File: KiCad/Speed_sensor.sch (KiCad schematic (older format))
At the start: 69 parts, among them J1 USB_B_Micro, J2 SWD, U1 BQ24040DSQR, U2 TP1941U, U3 ST1PS02, U4 nRF52832-QFxx, U5 LIS2DH12, Y1 32,768kHz, Y2 32MHz

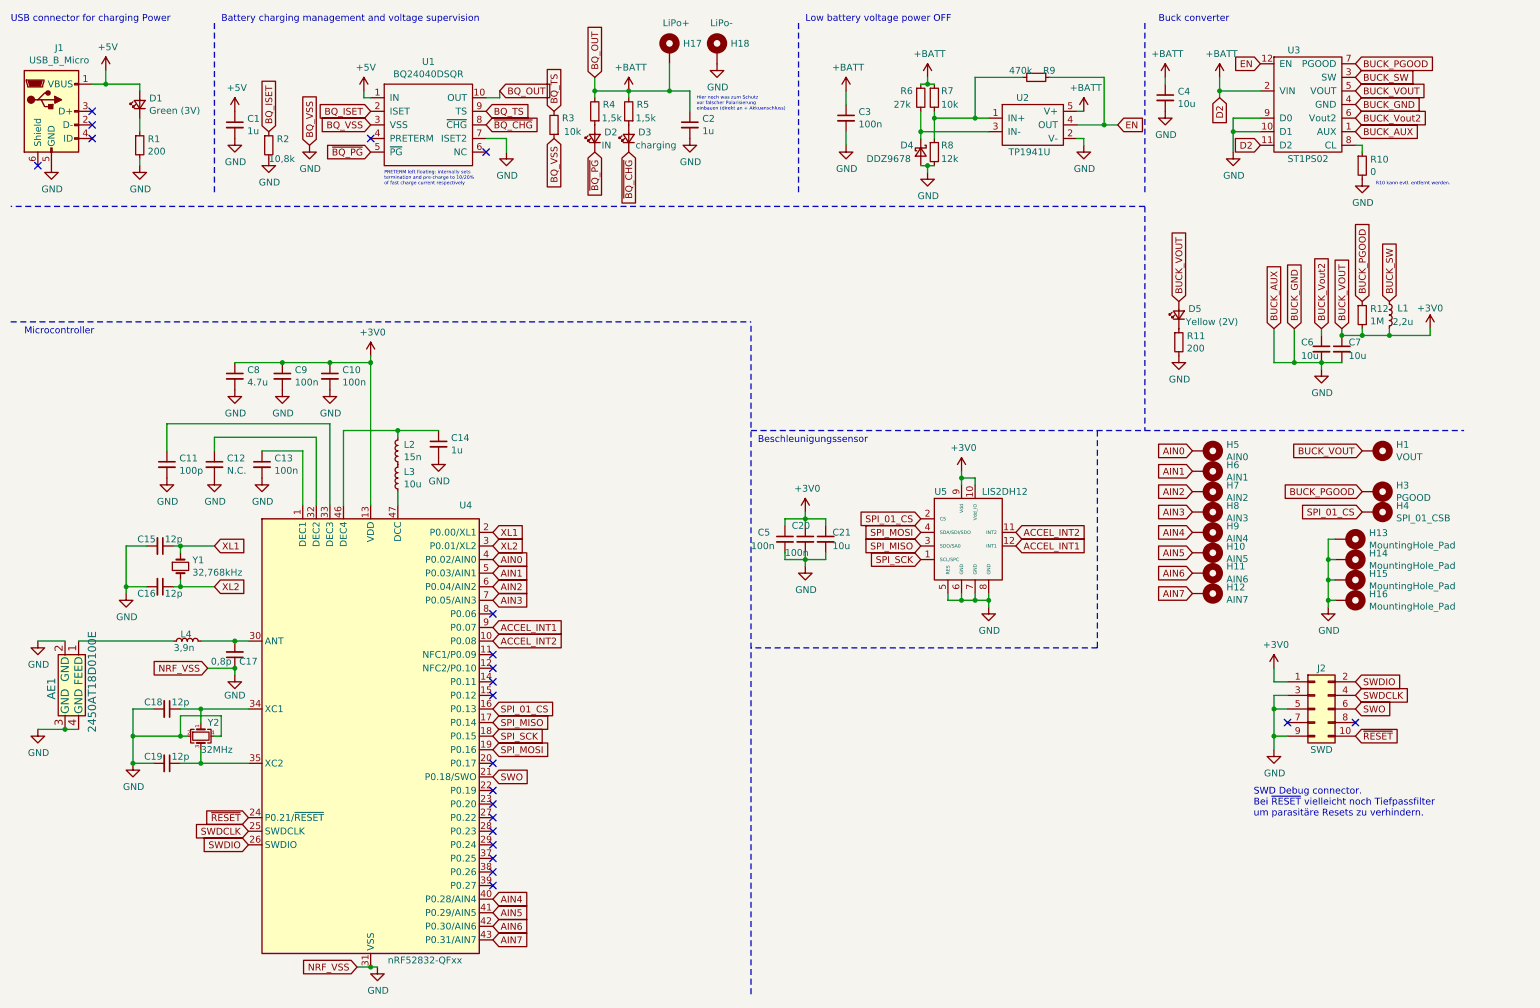
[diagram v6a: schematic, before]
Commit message: changed some labels in the .sch so all power stuff is labeled correctly
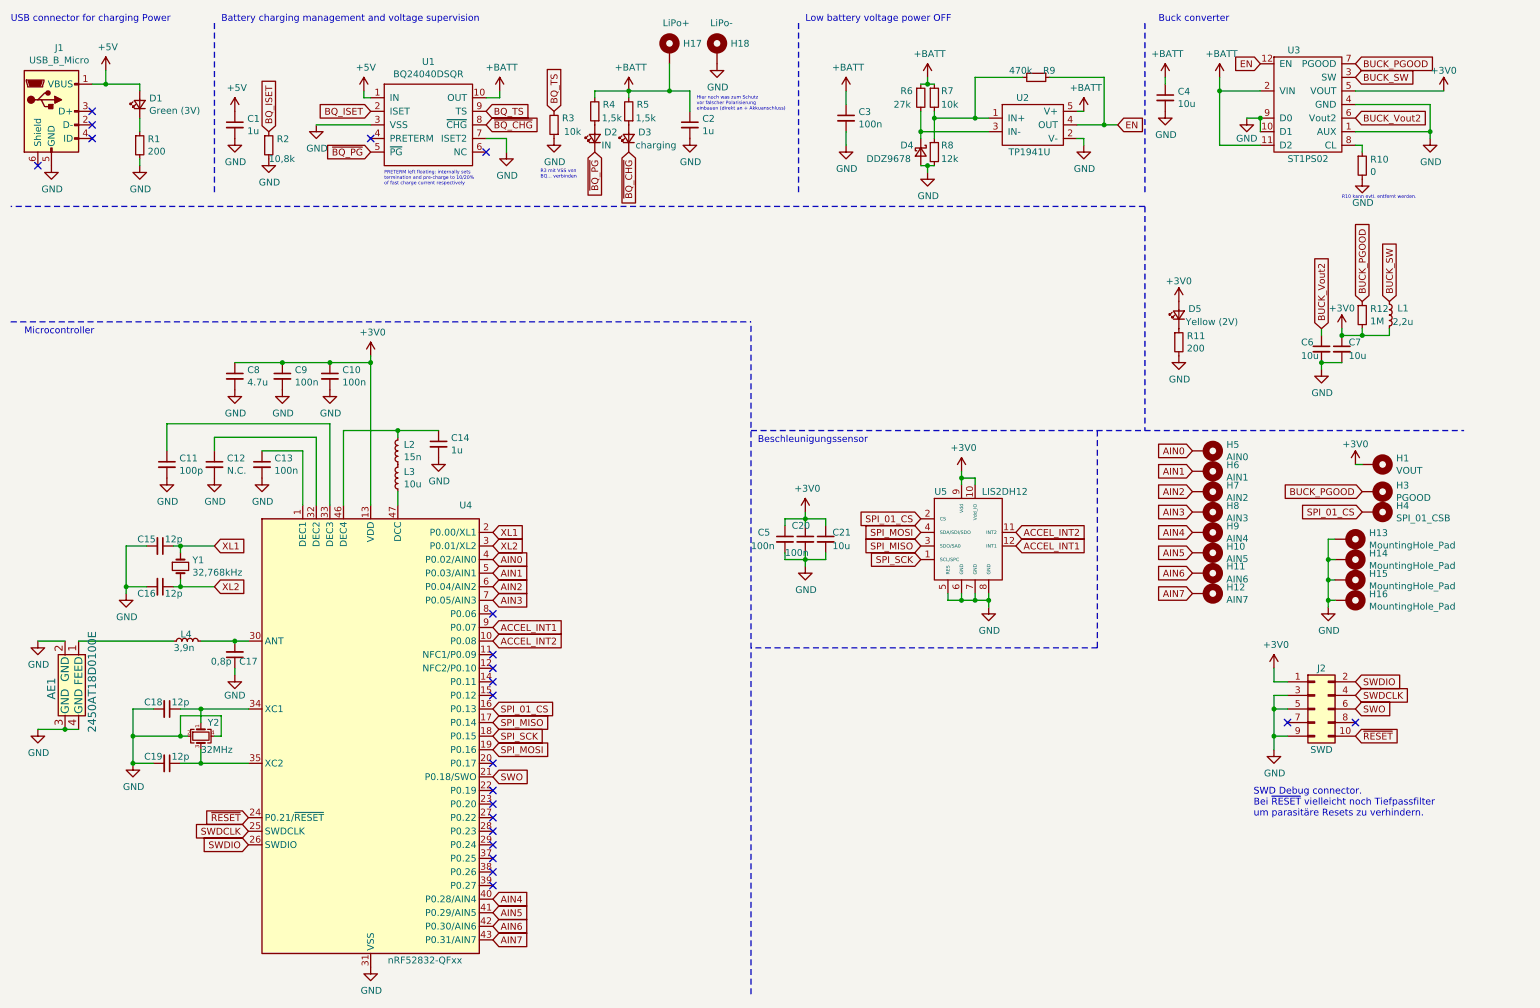
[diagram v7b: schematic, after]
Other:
- note added: "R3 mit VSS von \nBQ... verbinden"
- moved on the sheet: H1
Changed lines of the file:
@@
 L power:GND #PWR0101
 U 1 1 60833A00
-P 3200 7550
-F 0 "#PWR0101" H 3200 7300 50  0001 C CNN
-F 1 "GND" H 3205 7377 50  0000 C CNN
-F 2 "" H 3200 7550 50  0001 C CNN
-F 3 "" H 3200 7550 50  0001 C CNN
-	1    3200 7550
+P 3150 7550
+F 0 "#PWR0101" H 3150 7300 50  0001 C CNN
+F 1 "GND" H 3155 7377 50  0000 C CNN
+F 2 "" H 3150 7550 50  0001 C CNN
+F 3 "" H 3150 7550 50  0001 C CNN
+	1    3150 7550
 	1    0    0    -1
 $EndComp
@@
 Text Notes 600  2900 0    50   ~ 0
 Microcontroller
-Text GLabel 10450 3750 0    50   Input ~ 0
-BUCK_VOUT
 Text GLabel 4050 5650 2    50   Input ~ 0
 SPI_01_CS
@@
 L Mechanical:MountingHole_Pad H1
 U 1 1 609B0299
-P 10550 3750
-F 0 "H1" V 10504 3900 50  0000 L CNN
-F 1 "VOUT" V 10595 3900 50  0000 L CNN
-F 2 "TestPoint:TestPoint_Loop_D1.80mm_Drill1.0mm_Beaded" H 10550 3750 50  0001 C CNN
-F 3 "~" H 10550 3750 50  0001 C CNN
-	1    10550 3750
+P 10550 3850
+F 0 "H1" V 10504 4000 50  0000 L CNN
+F 1 "VOUT" V 10595 4000 50  0000 L CNN
+F 2 "TestPoint:TestPoint_Loop_D1.80mm_Drill1.0mm_Beaded" H 10550 3850 50  0001 C CNN
+F 3 "~" H 10550 3850 50  0001 C CNN
+	1    10550 3850
 	0    1    1    0
 $EndComp
@@
 Text GLabel 10400 5650 2    50   Input ~ 0
 SWO
-Text GLabel 9700 1500 0    50   Input ~ 0
-D2
 Text GLabel 9700 900  0    50   Input ~ 0
 EN
@@
 Text Notes 8950 600  0    50   ~ 0
 Buck converter
-Text GLabel 9400 1150 3    50   Input ~ 0
-D2
 $Comp
 L power:GND #PWR?
 U 1 1 609EC4A9
-P 9500 1550
+P 9600 1300
 AR Path="/608A57BF/609EC4A9" Ref="#PWR?"  Part="1"
 AR Path="/609EC4A9" Ref="#PWR029"  Part="1"
-F 0 "#PWR029" H 9500 1300 50  0001 C CNN
-F 1 "GND" H 9505 1377 50  0000 C CNN
-F 2 "" H 9500 1550 50  0001 C CNN
-F 3 "" H 9500 1550 50  0001 C CNN
-	1    9500 1550
-	1    0    0    -1
-$EndComp
-Wire Wire Line
-	9500 1400 9700 1400
-Wire Wire Line
-	9500 1300 9500 1400
-Connection ~ 9500 1400
-Wire Wire Line
-	9500 1400 9500 1550
-Text GLabel 10400 1100 2    50   Input ~ 0
-BUCK_VOUT
-Text GLabel 9100 2650 1    50   Input ~ 0
-BUCK_VOUT
-Wire Wire Line
-	9500 1300 9700 1300
+F 0 "#PWR029" H 9600 1050 50  0001 C CNN
+F 1 "GND" H 9600 1150 50  0000 C CNN
+F 2 "" H 9600 1300 50  0001 C CNN
+F 3 "" H 9600 1300 50  0001 C CNN
+	1    9600 1300
+	1    0    0    -1
+$EndComp
 Wire Wire Line
 	9400 1000 9400 1100
 Wire Wire Line
 	9400 1100 9700 1100
-Connection ~ 9400 1100
-Wire Wire Line
-	9400 1100 9400 1150
 $Comp
 L Device:C_Small C?
@@
 Text GLabel 10400 1000 2    50   Input ~ 0
 BUCK_SW
-Text GLabel 10400 1200 2    50   Input ~ 0
-BUCK_GND
 Text GLabel 10400 1300 2    50   Input ~ 0
 BUCK_Vout2
-Text GLabel 10400 1400 2    50   Input ~ 0
-BUCK_AUX
 $Comp
 L Device:R_Small R?
@@
 L power:GND #PWR09
 U 1 1 608BC5E0
-P 2700 1500
-F 0 "#PWR09" H 2700 1250 50  0001 C CNN
-F 1 "GND" H 2705 1327 50  0000 C CNN
-F 2 "" H 2700 1500 50  0001 C CNN
-F 3 "" H 2700 1500 50  0001 C CNN
-	1    2700 1500
-	1    0    0    -1
-$EndComp
-Text GLabel 4100 1100 2    50   Input ~ 0
-BQ_OUT
+P 2750 1350
+F 0 "#PWR09" H 2750 1100 50  0001 C CNN
+F 1 "GND" H 2755 1177 50  0000 C CNN
+F 2 "" H 2750 1350 50  0001 C CNN
+F 3 "" H 2750 1350 50  0001 C CNN
+	1    2750 1350
+	1    0    0    -1
+$EndComp
 Text GLabel 4000 1250 2    50   Input ~ 0
 BQ_TS
@@
 Wire Wire Line
 	4150 1450 4000 1450
-Text GLabel 3150 1350 0    50   Input ~ 0
-BQ_VSS
-Text GLabel 2700 1500 1    50   Input ~ 0
-BQ_VSS
-Text GLabel 4500 1450 3    50   Input ~ 0
-BQ_VSS
 Text GLabel 4500 1250 1    50   Input ~ 0
 BQ_TS
@@
 	-1   0    0    1
 $EndComp
-Text GLabel 4800 1000 1    50   Input ~ 0
-BQ_OUT
 Text GLabel 5050 1550 3    50   Input ~ 0
 ~BQ_CHG~
@@
 $EndComp
 Wire Wire Line
-	4800 1000 4800 1100
-Wire Wire Line
 	4800 1100 5050 1100
 Wire Wire Line
 	5050 1100 5050 1150
-Connection ~ 4800 1100
 Wire Wire Line
 	4800 1100 4800 1150
@@
 	1900 5150 2150 5150
 Connection ~ 2150 5150
-Text GLabel 3050 7550 0    50   Input ~ 0
-NRF_VSS
-Wire Wire Line
-	3050 7550 3150 7550
-Connection ~ 3150 7550
-Wire Wire Line
-	3150 7550 3200 7550
-Text GLabel 1950 5350 0    50   Input ~ 0
-NRF_VSS
 Wire Wire Line
 	2150 5350 2150 5400
-Wire Wire Line
-	2150 5350 1950 5350
-Connection ~ 2150 5350
 Wire Notes Line
 	2000 600  2000 1850
@@
 Text GLabel 10650 2650 1    50   Input ~ 0
 BUCK_SW
-Text GLabel 10300 2850 1    50   Input ~ 0
-BUCK_VOUT
-Text GLabel 9950 2850 1    50   Input ~ 0
-BUCK_GND
 Text GLabel 10150 2850 1    50   Input ~ 0
 BUCK_Vout2
@@
 L power:+3V0 #PWR033
 U 1 1 60CABFF4
-P 10950 2850
-F 0 "#PWR033" H 10950 2700 50  0001 C CNN
-F 1 "+3V0" H 10950 3000 50  0000 C CNN
-F 2 "" H 10950 2850 50  0001 C CNN
-F 3 "" H 10950 2850 50  0001 C CNN
-	1    10950 2850
-	1    0    0    -1
-$EndComp
-Wire Wire Line
-	10950 2850 10950 2900
+P 10300 2850
+F 0 "#PWR033" H 10300 2700 50  0001 C CNN
+F 1 "+3V0" H 10300 3000 50  0000 C CNN
+F 2 "" H 10300 2850 50  0001 C CNN
+F 3 "" H 10300 2850 50  0001 C CNN
+	1    10300 2850
+	1    0    0    -1
+$EndComp
 Connection ~ 10300 2900
-Wire Wire Line
-	9950 2850 9950 3100
 $Comp
 L Device:L_Small L1
@@
 	10300 2900 10450 2900
 Connection ~ 10450 2900
-Connection ~ 10650 2900
 Wire Wire Line
 	10450 2900 10650 2900
-Wire Wire Line
-	10650 2900 10950 2900
-Connection ~ 9950 3100
-Wire Wire Line
-	9950 3100 10150 3100
-Text GLabel 9800 2850 1    50   Input ~ 0
-BUCK_AUX
-Wire Wire Line
-	9800 2850 9800 3100
-Wire Wire Line
-	9800 3100 9950 3100
 Text GLabel 4050 7050 2    50   Input ~ 0
 AIN4
@@
 Wire Wire Line
 	1750 5700 2050 5700
-Text Notes 10550 1800 0    25   ~ 0
+Text Notes 10300 1900 0    25   ~ 0
 R10 kann evtl. entfernt werden.
 $Comp
@@
 Wire Wire Line
 	4100 1150 4000 1150
+$Comp
+L power:+BATT #PWR037
+U 1 1 60A5CE9C
+P 4100 1100
+AR Path="/60A5CE9C" Ref="#PWR037"  Part="1"
+AR Path="/608A57BF/60A5CE9C" Ref="#PWR?"  Part="1"
+F 0 "#PWR037" H 4100 950 50  0001 C CNN
+F 1 "+BATT" H 4115 1273 50  0000 C CNN
+F 2 "" H 4100 1100 50  0001 C CNN
+F 3 "" H 4100 1100 50  0001 C CNN
+	1    4100 1100
+	1    0    0    -1
+$EndComp
+$Comp
+L power:+3V0 #PWR040
+U 1 1 60A5D75E
+P 11050 1100
+F 0 "#PWR040" H 11050 950 50  0001 C CNN
+F 1 "+3V0" H 11050 1250 50  0000 C CNN
+F 2 "" H 11050 1100 50  0001 C CNN
+F 3 "" H 11050 1100 50  0001 C CNN
+	1    11050 1100
+	1    0    0    -1
+$EndComp
+Wire Wire Line
+	10400 1100 11050 1100
+$Comp
+L power:+3V0 #PWR038
+U 1 1 60A6E034
+P 9100 2650
+F 0 "#PWR038" H 9100 2500 50  0001 C CNN
+F 1 "+3V0" H 9100 2800 50  0000 C CNN
+F 2 "" H 9100 2650 50  0001 C CNN
+F 3 "" H 9100 2650 50  0001 C CNN
+	1    9100 2650
+	1    0    0    -1
+$EndComp
+$Comp
+L power:+3V0 #PWR039
+U 1 1 60A6F470
+P 10400 3850
+F 0 "#PWR039" H 10400 3700 50  0001 C CNN
+F 1 "+3V0" H 10400 4000 50  0000 C CNN
+F 2 "" H 10400 3850 50  0001 C CNN
+F 3 "" H 10400 3850 50  0001 C CNN
+	1    10400 3850
+	1    0    0    -1
+$EndComp
+Wire Wire Line
+	10400 3850 10450 3850
+Wire Wire Line
+	2750 1350 3150 1350
+$Comp
+L power:GND #PWR041
+U 1 1 60A8BA9E
+P 4500 1450
+F 0 "#PWR041" H 4500 1200 50  0001 C CNN
+F 1 "GND" H 4505 1277 50  0000 C CNN
+F 2 "" H 4500 1450 50  0001 C CNN
+F 3 "" H 4500 1450 50  0001 C CNN
+	1    4500 1450
+	1    0    0    -1
+$EndComp
+Text Notes 4400 1750 0    25   ~ 0
+R3 mit VSS von \nBQ... verbinden
+$Comp
+L power:GND #PWR?
+U 1 1 60A8E087
+P 10950 1450
+AR Path="/608A57BF/60A8E087" Ref="#PWR?"  Part="1"
+AR Path="/60A8E087" Ref="#PWR042"  Part="1"
+F 0 "#PWR042" H 10950 1200 50  0001 C CNN
+F 1 "GND" H 10955 1277 50  0000 C CNN
+F 2 "" H 10950 1450 50  0001 C CNN
+F 3 "" H 10950 1450 50  0001 C CNN
+	1    10950 1450
+	1    0    0    -1
+$EndComp
+Wire Wire Line
+	10400 1200 10950 1200
+Wire Wire Line
+	10950 1200 10950 1400
+Wire Wire Line
+	10400 1400 10950 1400
+Connection ~ 10950 1400
+Wire Wire Line
+	10950 1400 10950 1450
+Wire Wire Line
+	9700 1400 9700 1300
+Wire Wire Line
+	9600 1300 9700 1300
+Connection ~ 9700 1300
+Wire Wire Line
+	9700 1500 9400 1500
+Wire Wire Line
+	9400 1500 9400 1100
+Connection ~ 9400 1100
 $EndSCHEMATC

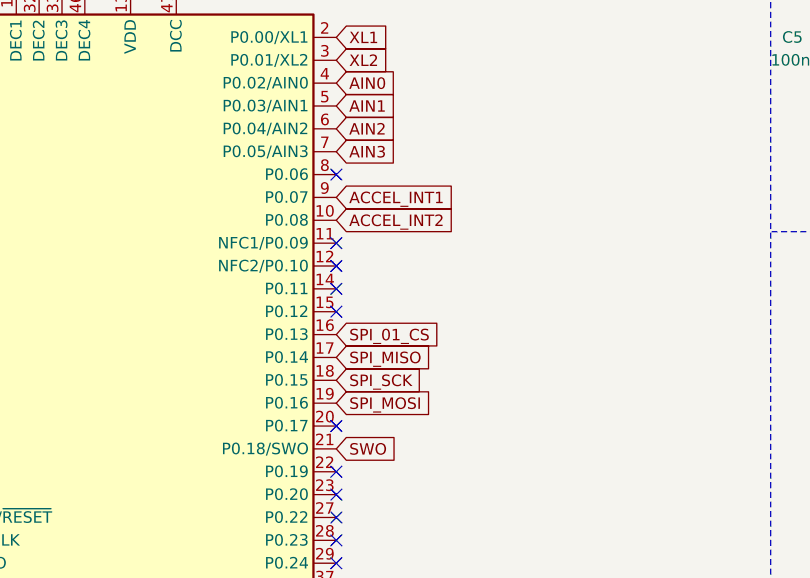
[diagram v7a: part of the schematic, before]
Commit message: changed which GPIO pins are used for SPI
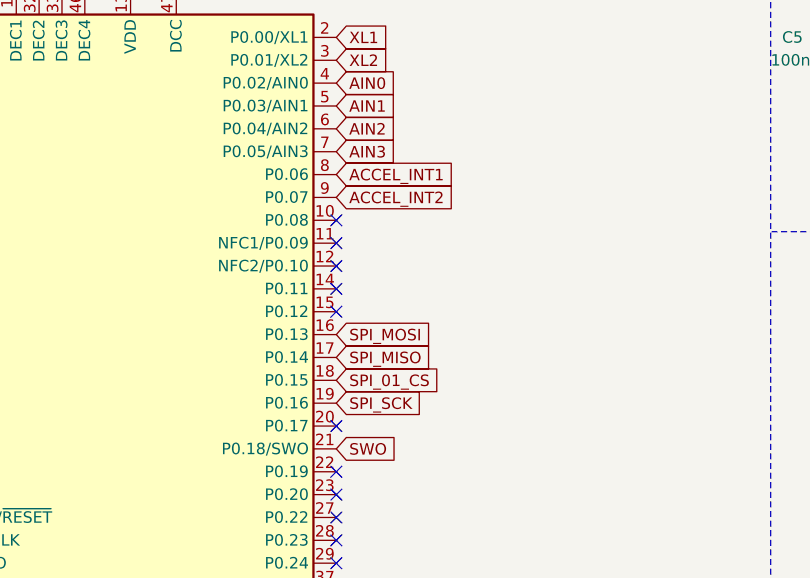
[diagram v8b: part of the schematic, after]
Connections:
- net ACCEL_INT1: now also U4.8 (P0.06); no longer U4.9 (P0.07)
- net ACCEL_INT2: now also U4.9 (P0.07); no longer U4.10 (P0.08)
- net SPI_01_CS: now also U4.18 (P0.15); no longer U4.16 (P0.13)
- net SPI_MOSI: now also U4.16 (P0.13); no longer U4.19 (P0.16)
- net SPI_SCK: now also U4.19 (P0.16); no longer U4.18 (P0.15)
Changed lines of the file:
@@
 Text Notes 600  2900 0    50   ~ 0
 Microcontroller
-Text GLabel 4050 5650 2    50   Input ~ 0
+Text GLabel 4050 5850 2    50   Input ~ 0
 SPI_01_CS
 Text GLabel 4050 5750 2    50   Input ~ 0
 SPI_MISO
-Text GLabel 4050 5950 2    50   Input ~ 0
+Text GLabel 4050 5650 2    50   Input ~ 0
 SPI_MOSI
 Text Notes 6000 3700 0    50   ~ 0
@@
 	0    1    1    0
 $EndComp
-Text GLabel 4050 5850 2    50   Input ~ 0
+Text GLabel 4050 5950 2    50   Input ~ 0
 SPI_SCK
 Text GLabel 4050 6150 2    50   Input ~ 0
@@
 Text GLabel 4050 4750 2    50   Input ~ 0
 AIN2
-Text GLabel 4050 4850 2    50   Input ~ 0
-AIN3
 Text GLabel 2000 4450 2    50   Input ~ 0
 XL1
@@
 Text GLabel 7200 4250 0    50   Input ~ 0
 SPI_01_CS
+Text GLabel 4050 4950 2    50   Input ~ 0
+ACCEL_INT1
 Text GLabel 4050 5050 2    50   Input ~ 0
-ACCEL_INT1
-Text GLabel 4050 5150 2    50   Input ~ 0
 ACCEL_INT2
 Text GLabel 7900 4450 2    50   Input ~ 0
@@
 Text GLabel 9200 4800 0    50   Input ~ 0
 AIN7
-NoConn ~ 4050 4950
 NoConn ~ 4050 5250
 NoConn ~ 4050 5350
@@
 	9400 1500 9400 1100
 Connection ~ 9400 1100
+NoConn ~ 4050 5150
+Text GLabel 4050 4850 2    50   Input ~ 0
+AIN3
 $EndSCHEMATC
